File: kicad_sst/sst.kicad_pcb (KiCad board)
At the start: 2 copper layers, 75 x 75.5 mm, 34 parts

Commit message: Updated pcb according to schematics
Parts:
- added R13: R, Resistor_THT:R_Axial_DIN0207_L6.3mm_D2.5mm_P7.62mm_Horizontal, F.Cu at (216.5, 68.6)
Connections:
- DD1 pad 24: GND -> Net-(DD1-PC1)
- DD1 pad 25: GND -> Net-(DD1-PC2)
- R5 pad 1: +2V5 -> GND
- R5 pad 3: GND -> +2V5
- R6 pad 1: +2V5 -> GND
- R6 pad 2: GND -> Net-(DD1-PC2)
- R6 pad 3: GND -> +2V5
- R7 pad 1: +2V5 -> GND
- R7 pad 2: GND -> Net-(DD1-PC1)
- R7 pad 3: GND -> +2V5
- R8 pad 1: +2V5 -> GND
- R8 pad 3: GND -> +2V5

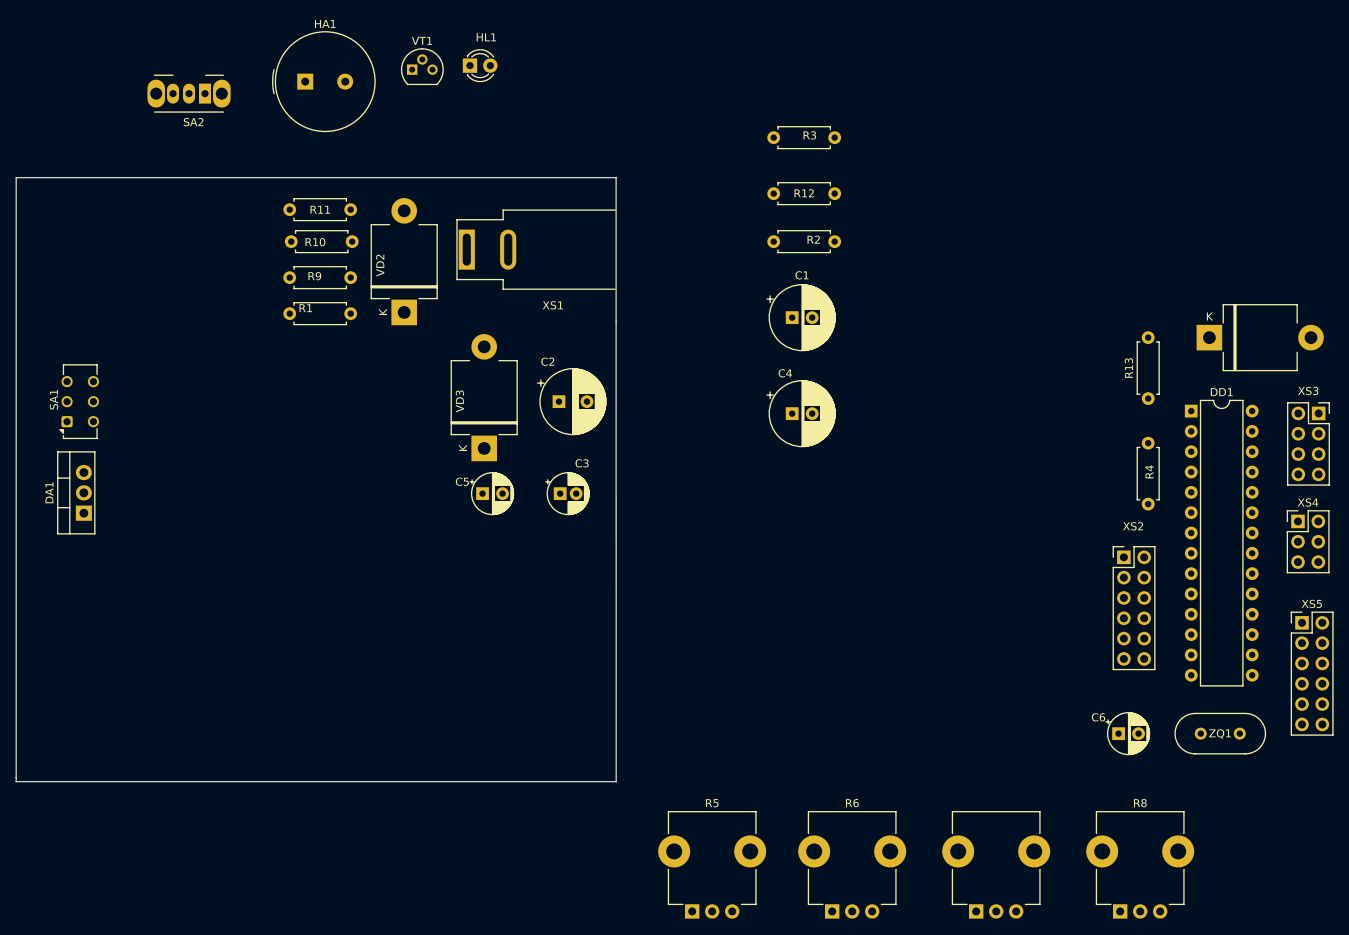
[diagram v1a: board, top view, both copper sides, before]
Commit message: Arranged components on PCB
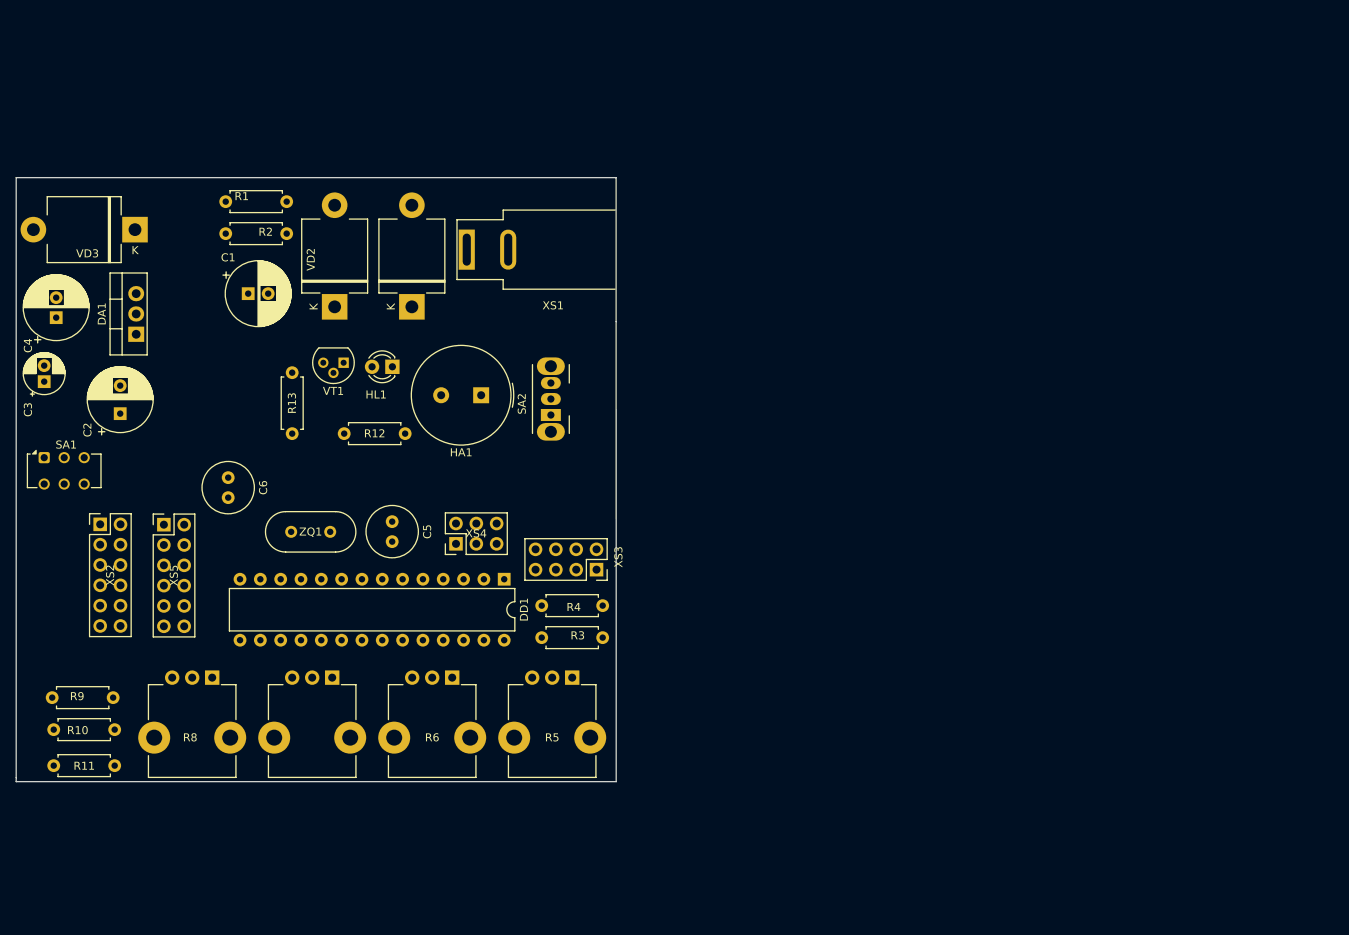
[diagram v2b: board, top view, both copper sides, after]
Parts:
- C5, C6: footprint Capacitor_THT:CP_Radial_D5.0mm_P2.50mm -> Capacitor_THT:C_Radial_D6.3mm_H5.0mm_P2.50mm
- moved XS5 142.8 mm to (93.5, 84.4)
- moved XS2 128.0 mm to (85.5, 84.3)
- moved R8 117.2 mm to (99.5, 103.5), turned to 180 degrees
- moved ZQ1 116.5 mm to (114.2, 85.3)
- moved C6 115.8 mm to (101.5, 78.5), turned to -90 degrees
- moved R13 107.0 mm to (109.5, 65.4), turned to -90 degrees
- moved XS4 105.3 mm to (130.0, 86.8), turned to 90 degrees
- moved VD1 99.8 mm to (124.5, 57.1), turned to 90 degrees
- moved C4 92.8 mm to (80.0, 58.5), turned to 90 degrees
- moved XS3 92.4 mm to (147.5, 90.0), turned to -90 degrees
- moved DD1 88.4 mm to (136.0, 91.2), turned to -90 degrees
- moved R7 85.6 mm to (114.5, 103.5), turned to 180 degrees
- moved R4 76.9 mm to (140.7, 94.5), turned to 0 degrees
- moved R11 75.5 mm to (79.7, 114.5)
- moved R3 68.9 mm to (140.7, 98.5)
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
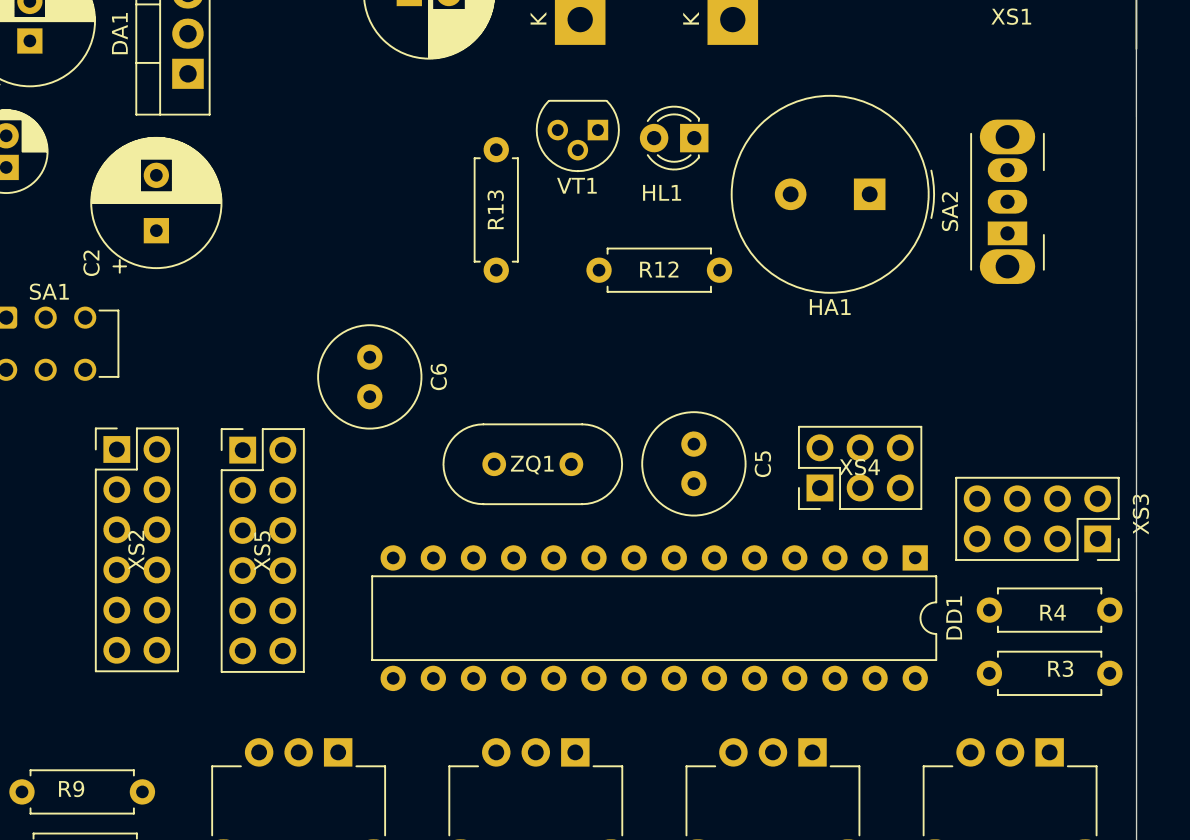
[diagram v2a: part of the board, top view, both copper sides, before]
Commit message: Rearranged components a little bit
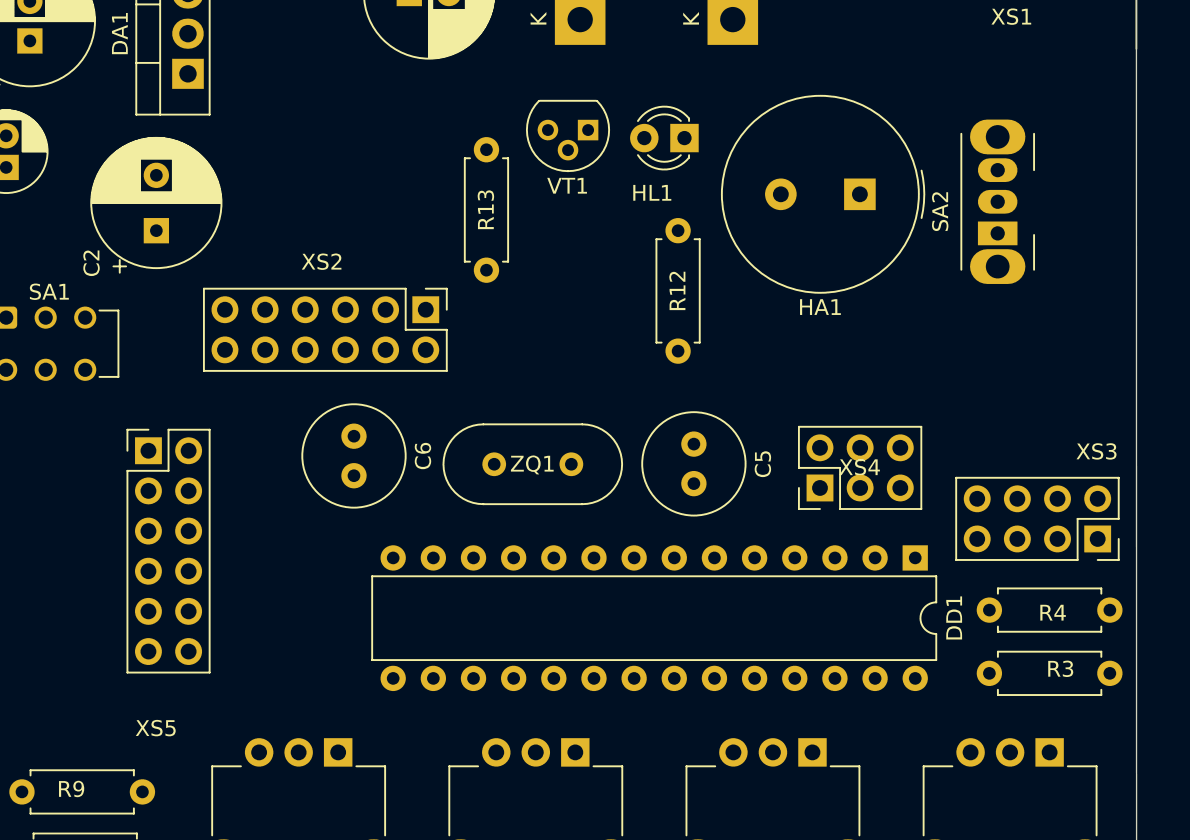
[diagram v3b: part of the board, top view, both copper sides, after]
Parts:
- moved XS2 21.4 mm to (105.0, 75.5), turned to -90 degrees
- moved XS5 5.96 mm to (87.5, 84.4)
- moved R12 5.59 mm to (121.0, 70.5), turned to -90 degrees
- moved C6 5.10 mm to (100.5, 83.5)
- moved HA1 0.62 mm to (132.5, 68.2)
- moved HL1 0.62 mm to (121.4, 64.6)
- moved R13 0.62 mm to (108.9, 65.4)
- moved SA2 0.62 mm to (141.2, 70.7)
- moved VT1 0.62 mm to (115.3, 64.1)

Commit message: Traced everything but power
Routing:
- net Net-(DD1-PB3): track 0.00 -> 68.3 mm
- net Net-(DD1-PC4): track 0.00 -> 62.9 mm
- net Net-(DD1-PD2): track 0.00 -> 62.0 mm, vias 0 -> 1
- net Net-(VD3-A): track 0.00 -> 60.8 mm
- net Net-(DD1-PB4): track 0.00 -> 53.4 mm
- net Net-(DD1-PD4): track 0.00 -> 48.9 mm, vias 0 -> 1
- net Net-(DD1-PD6): track 0.00 -> 42.6 mm, vias 0 -> 1
- net Net-(DD1-PD5): track 0.00 -> 40.4 mm, vias 0 -> 1
- net Net-(DD1-EPB5): track 0.00 -> 36.3 mm
- net Net-(DD1-PD1): track 0.00 -> 31.8 mm
- net Net-(DA1-OUT): track 0.00 -> 29.4 mm
- net Net-(DD1-PC0): track 0.00 -> 29.0 mm
- net Net-(DD1-PB2): track 0.00 -> 26.2 mm
- net Net-(DA1-IN): track 0.00 -> 25.2 mm
- net Net-(DD1-PD0): track 0.00 -> 25.2 mm, vias 0 -> 1
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
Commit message: traced pcb
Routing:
- net GND: track 0.00 -> 368.1 mm, vias 0 -> 3
- net +5V: track 0.00 -> 183.4 mm, vias 0 -> 1
- net +2V5: track 0.00 -> 154.7 mm
- net +BATT: track 0.00 -> 101.3 mm, vias 0 -> 1
- net Net-(DD1-PD6): track 42.6 -> 46.9 mm
- net Net-(DD1-PD7): track 17.3 -> 18.1 mm
- net Net-(HA1--): track 17.5 -> 18.2 mm
